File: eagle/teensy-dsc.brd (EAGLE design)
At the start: 45.4 x 65.1 mm, 27 parts, among them J1 RJ11-6PTH, J2 RJ11-6PTH, J3 RJ45-8PTH, J4 POWER_JACKPTH, M1 XBEERX-VN, Q1 IRLML6344, X1 STEREOJACK, X2 STEREOJACK

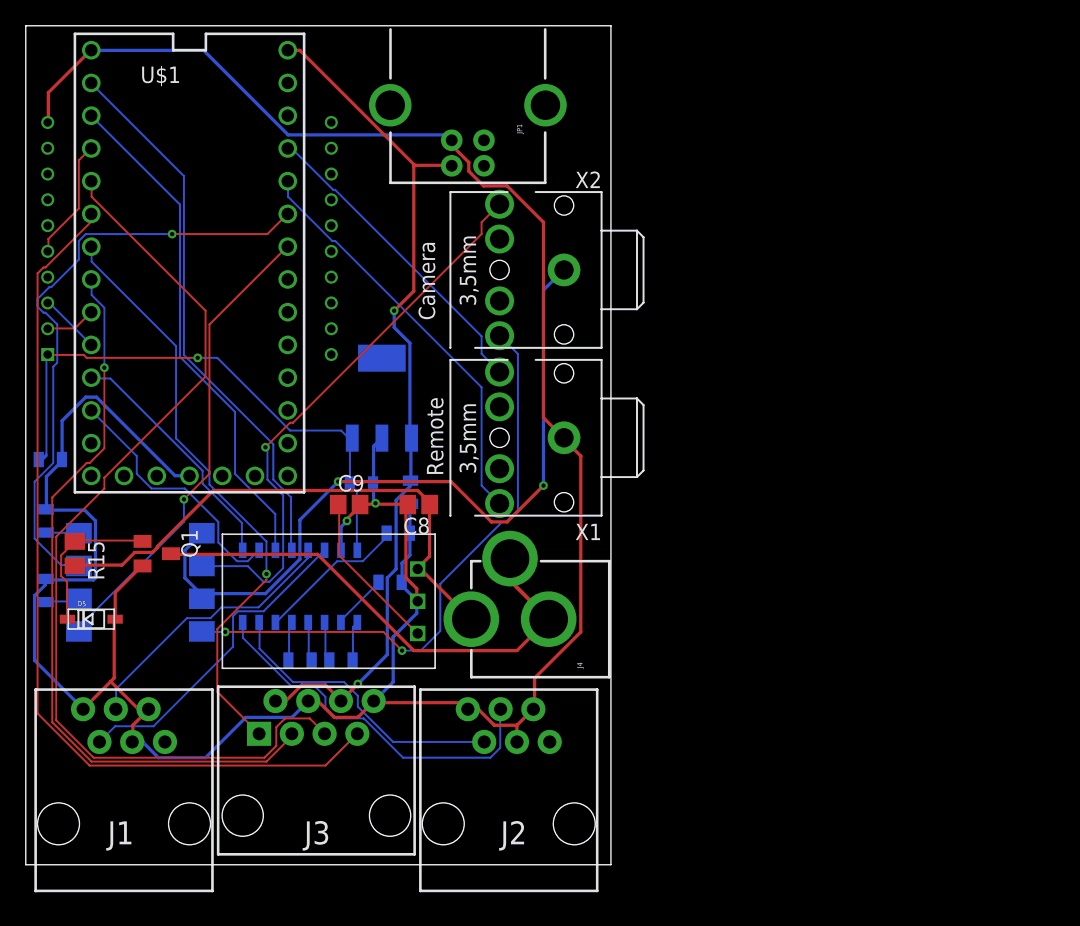
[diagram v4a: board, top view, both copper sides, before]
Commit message: Fix power error in .sch Update board to theoretically fit in CU-789 box
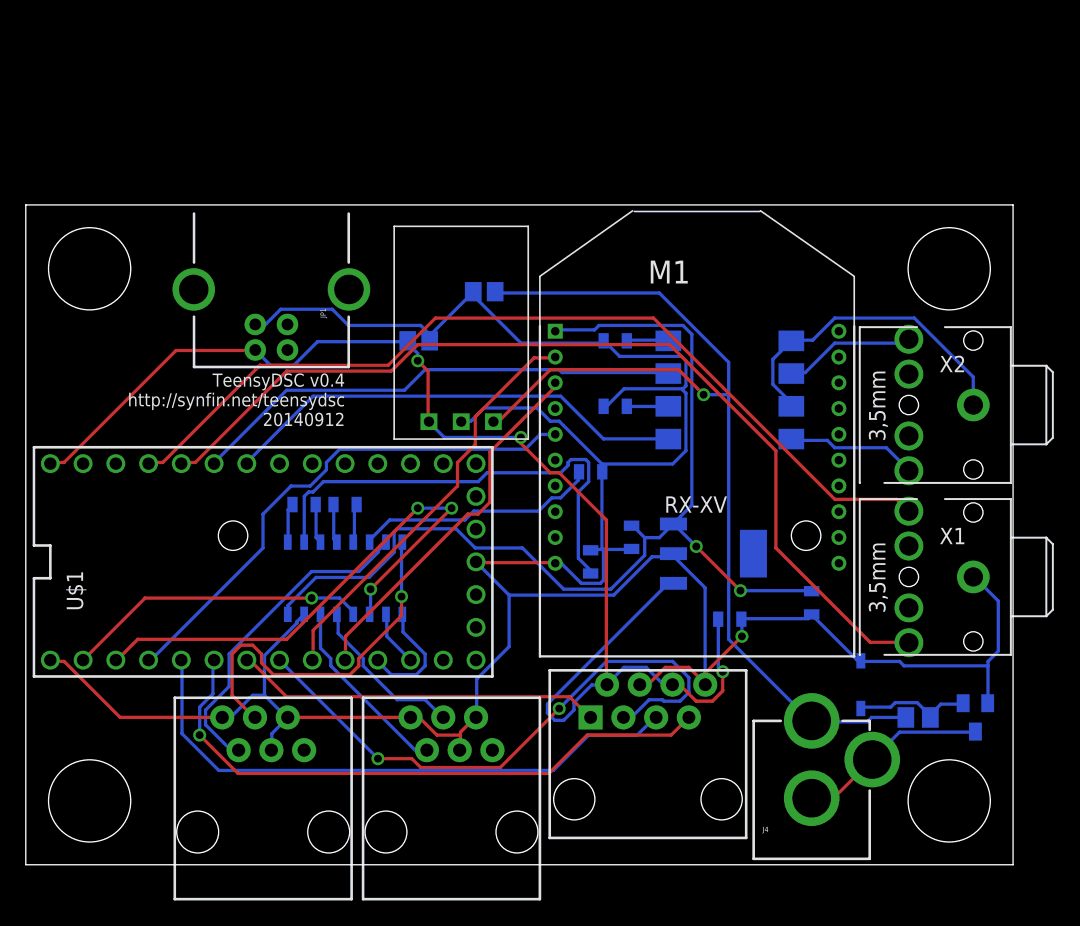
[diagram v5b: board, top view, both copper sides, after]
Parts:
- moved R15 66.6 mm to (69.2, 11.4), flipped to the bottom, turned to 0 degrees
- moved Q1 64.8 mm to (73.7, 11.4), flipped to the bottom, turned to 180 degrees
- moved C1 60.1 mm to (61.0, 20.3), turned to 270 degrees
- moved D5 59.9 mm to (64.8, 14.0), flipped to the bottom, turned to 90 degrees
- moved OK1 48.1 mm to (54.6, 36.8)
- moved R1 46.4 mm to (45.7, 35.6), turned to 180 degrees
- moved R2 46.3 mm to (45.7, 40.6), turned to 180 degrees
- moved M1 43.6 mm to (54.6, 31.1), flipped to the top, turned to 0 degrees
- moved X1 33.5 mm to (76.2, 22.2)
- moved X2 33.4 mm to (76.2, 35.6)
- moved U$3 28.4 mm to (53.3, 24.1), turned to 90 degrees
- moved C2 26.6 mm to (54.6, 19.1), turned to 0 degrees
- moved J3 25.7 mm to (48.3, 5.08)
- moved J1 25.4 mm to (27.9, 2.54)
- moved J4 25.0 mm to (61.0, -2.54), turned to 0 degrees
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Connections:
- removed net 12V: C2.2, J3.2, J3.6, JP1.VBUS, U$1.VIN, U$3.1
- net 5V: now also C2.2, J3.2, J3.6, JP1.VBUS, U$1.VIN, U$3.1
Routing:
- net 5V: track 12.6 -> 107.0 mm, vias 0 -> 3
- net 12V: track 67.6 -> 0.00 mm, vias 2 -> 0
- net SW2: track 24.4 -> 69.9 mm
- net SW1: track 31.9 -> 74.3 mm
- net +12V: track 41.8 -> 79.2 mm, vias 0 -> 1
- net FOCUS: track 45.9 -> 10.2 mm, vias 2 -> 0
- net 3.3V: track 44.0 -> 79.5 mm, vias 1 -> 2
- net SHUTTER: track 43.7 -> 10.2 mm, vias 1 -> 0
- net SHUTTER-GND: track 58.3 -> 25.2 mm, vias 2 -> 0
- net N$6: track 4.32 -> 36.4 mm
- net XBEE_RST: track 9.41 -> 40.8 mm
- net CHAN-B-ALT/DEC: track 74.9 -> 45.4 mm
- net XBEE_OUT: track 3.90 -> 32.3 mm
- net GND_MAIN: track 39.4 -> 14.8 mm
- net XBEE_IN: track 4.74 -> 28.8 mm
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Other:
- board size 45.4 x 65.1 mm -> 76.6 x 51.2 mm
- board text added: "TeensyDSC v0.4 http://synfin.net/teensydsc 20140912"
- board text removed: "Camera"
- board text removed: "J3"
- board text removed: "Remote"
- board text removed: "Teensy DSC v0.2 http://synfin.net/teensydsc 20140908"
